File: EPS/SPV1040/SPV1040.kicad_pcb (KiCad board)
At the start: 2 copper layers, 53.5 x 37.5 mm, 20 parts, among them J1 Screw_Terminal_01x02, J2 Screw_Terminal_01x02, U1 SPV1040

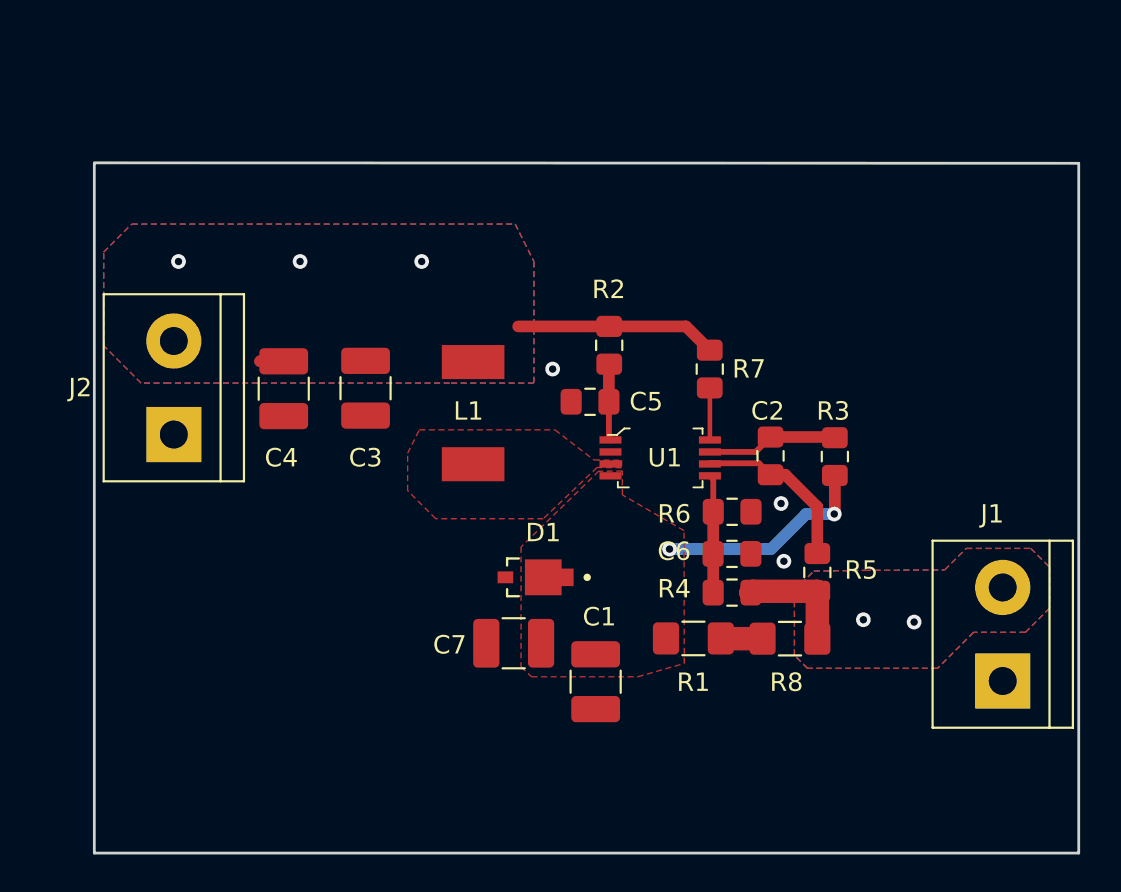
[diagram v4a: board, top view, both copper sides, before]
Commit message: completing charging circuit L6924D
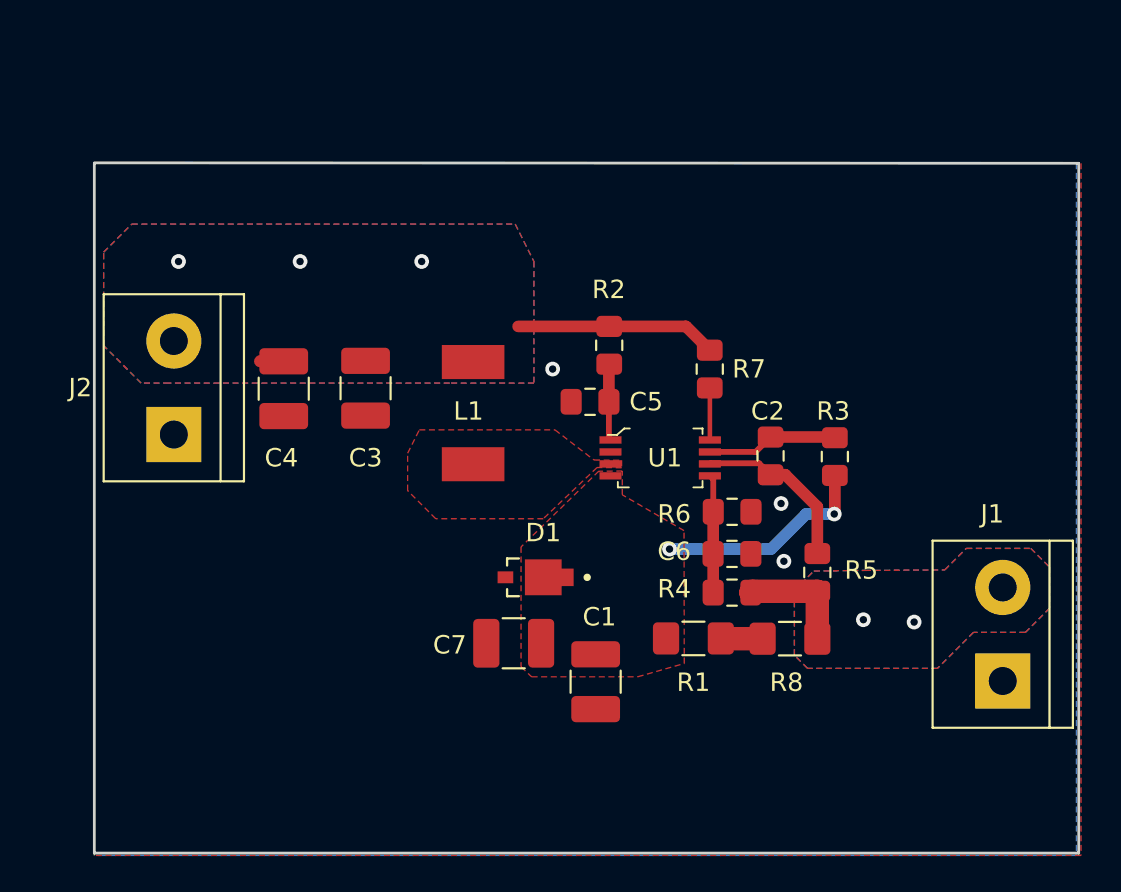
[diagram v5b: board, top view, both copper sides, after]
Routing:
- added copper zone on B.Cu, net GND
- added copper zone on F.Cu, net GND
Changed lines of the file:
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@@
     (visible_elements 7FFFFFFF)
     (pcbplotparams
-      (layerselection 0x010fc_ffffffff)
+      (layerselection 0x01000_ffffffff)
       (usegerberextensions false)
       (usegerberattributes false)
@@
       (outputformat 1)
       (mirror false)
-      (drillshape 1)
+      (drillshape 0)
       (scaleselection 1)
-      (outputdirectory ""))
+      (outputdirectory "D:/Juan_Ayala/"))
   )
   (net 0 "")
@@
       )
     )
+  )
+  (zone (net 2) (net_name GND) (layer F.Cu) (hatch edge 0.508)
+    (connect_pads yes (clearance 0))
+    (min_thickness 0.254)
+    (fill yes (arc_segments 16) (thermal_gap 0.508) (thermal_bridge_width 0.508))
+    (polygon
+      (pts
+        (xy 46.228 41.91) (xy 99.822 41.91) (xy 99.822 79.502) (xy 46.228 79.502)
+      )
+    )
+  )
+  (zone (net 2) (net_name GND) (layer B.Cu) (hatch edge 0.508)
+    (connect_pads yes (clearance 0))
+    (min_thickness 0.254)
+    (fill yes (arc_segments 16) (thermal_gap 0.508) (thermal_bridge_width 0.508))
+    (polygon
+      (pts
+        (xy 46.228 41.91) (xy 99.568 41.91) (xy 99.568 79.502) (xy 46.736 79.502) (xy 46.228 79.502)
+        (xy 46.228 79.248)
+      )
+    )

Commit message: changing screw terminal footprint for smaller whole. And smaller track width for more 10mils
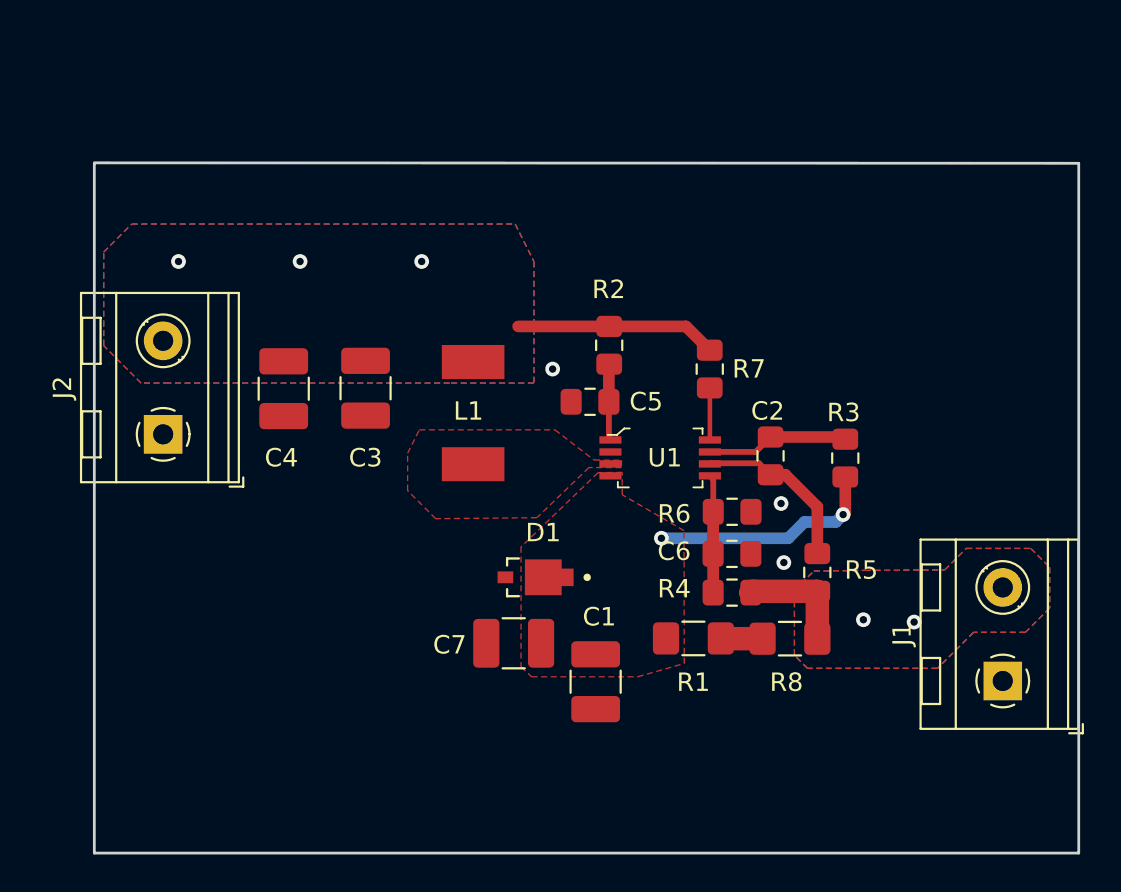
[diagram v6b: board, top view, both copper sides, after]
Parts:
- J1, J2: footprint TerminalBlock:TerminalBlock_bornier-2_P5.08mm -> TerminalBlock_RND:TerminalBlock_RND_205-00232_1x02_P5.08mm_Horizontal
- moved J2 0.58 mm to (50.0, 56.6)
- moved R3 0.57 mm to (87.0, 57.9)
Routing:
- net Net-(C1-Pad2): track 12.6 -> 13.2 mm
- removed copper zone on B.Cu, net GND
- removed copper zone on F.Cu, net GND
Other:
- net class Default: clearance 0.2032 -> 0.254
- rule trace_clearance: 0.2032 -> 0.254
- rule trace_min: 0.2 -> 0.1
